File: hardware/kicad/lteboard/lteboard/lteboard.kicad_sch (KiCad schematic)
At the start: 0 parts

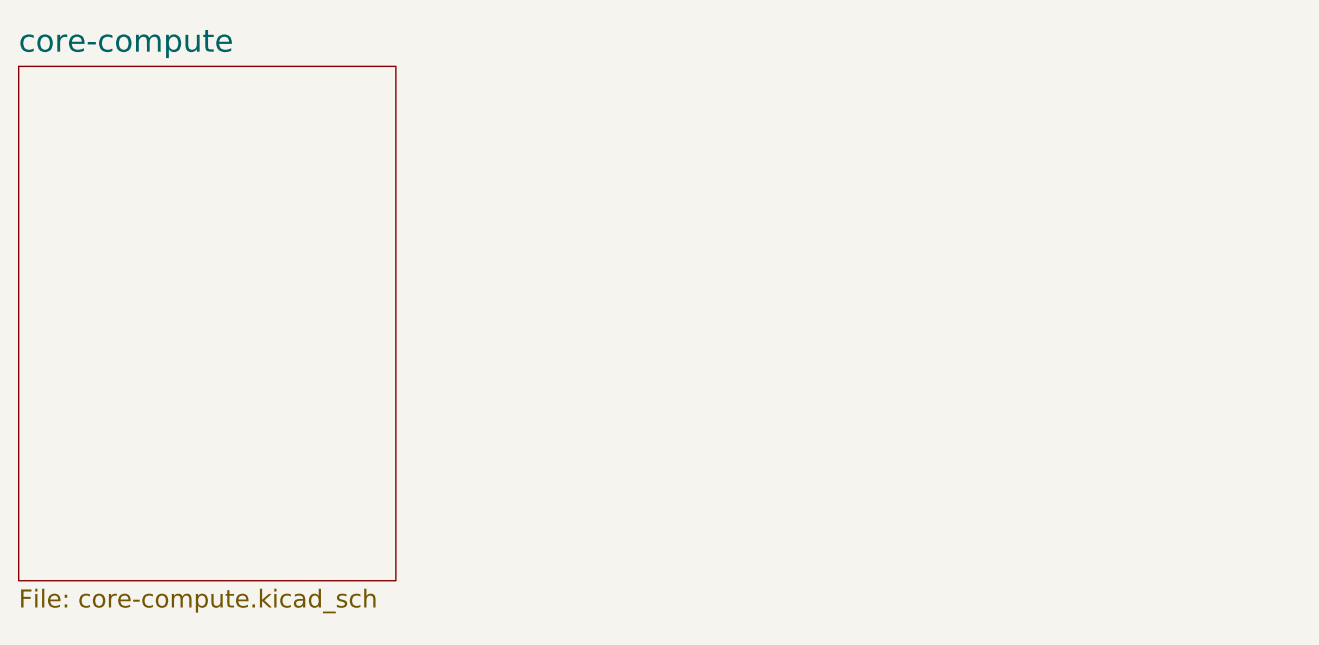
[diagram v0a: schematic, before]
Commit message: status-indication: fix GND_LOGIC scope, add sheet + PCA9535PW component placement
- core-compute.kicad_sch: converted 5 local GND_LOGIC labels to global_label,
  matching the project convention (global labels reserved for GND_LOGIC only).
  Local scope would have left the new status-indication sheet's GND_LOGIC
  electrically isolated from the MCU's ground - a real bug caught before wiring.
- lteboard.kicad_sch / lteboard.kicad_pro: added the new status_indication
  hierarchical sheet as LTEBOARD's second child sheet.
- status_indication.kicad_sch: new sheet, components placed (PCA9535PW I2C GPIO
  expander, 6x status LED, 6x 680R LED resistor, 2x 4.7k I2C pull-up, 1x 10k INT
  pull-up, 1x 100nF decoupling cap) - not yet wired.
- Added PCA9535PW symbol/footprint/3D-model library under hardware/kicad/lteboard/libs/
  (not in KiCad's default library) and the project's sym-lib-table pointing to it,
  fixed to use ${KIPRJMOD}-relative path instead of an absolute machine path.

Deliberately not included: uncommitted analog-io changes still sitting in this
working tree (power.kicad_sch, digital_inputs.kicad_sch, relay_outputs.kicad_sch,
ioboard.kicad_pro/kicad_sch, analog_io.kicad_sch) - this branch forked before
analog-io merged, and that content already lives on the analog-io branch.
Committing it here too would duplicate it across two branches.

Co-Authored-By: Claude Sonnet 5 <noreply@anthropic.com>
Claude-Session: https://claude.ai/code/session_011Mk4ACKLUzGL8p2SUjrweQ
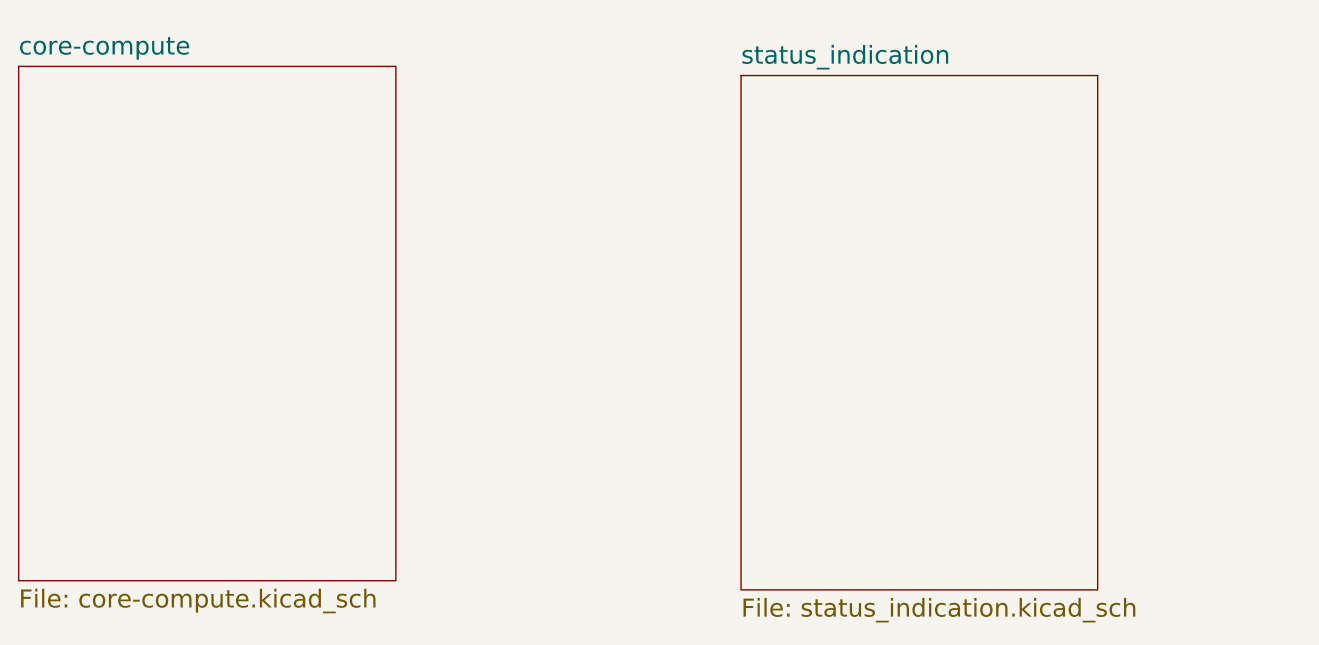
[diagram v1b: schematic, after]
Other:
- added sheet status_indication (status_indication.kicad_sch)
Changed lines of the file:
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@@
 		)
 		(property "Sheetname" "core-compute"
-			(at 35.56 36.7734 0)
+			(at 35.56 37.0234 0)
 			(effects
 				(font
-					(size 2.5 2.5)
+					(size 2 2)
 				)
 				(justify left bottom)
@@
 				)
 			)
+		)
+	)
+	(sheet
+		(at 115.824 39.116)
+		(size 39.624 57.15)
+		(exclude_from_sim no)
+		(in_bom yes)
+		(on_board yes)
+		(dnp no)
+		(fields_autoplaced yes)
+		(stroke
+			(width 0.1524)
+			(type solid)
+		)
+		(fill
+			(color 0 0 0 0.0000)
+		)
+		(property "Sheetname" "status_indication"
+			(at 115.824 38.0394 0)
+			(effects
+				(font
+					(size 2 2)
+				)
+				(justify left bottom)
+			)
+		)
+		(property "Sheetfile" "status_indication.kicad_sch"
+			(at 115.824 97.1426 0)
+			(effects
+				(font
+					(size 2 2)
+				)
+				(justify left top)
+			)
+		)
+		(instances
+			(project "lteboard"
+				(path "/e3cbe890-827c-4e3e-bf4e-d33595c4d0b3"
+					(page "3")
+				)
+			)

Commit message: status-indication: complete schematic capture, cross-sheet wiring, docs, and BOM
- status_indication.kicad_sch: full wiring completed (address straps, power/ground,
  I2C pull-ups, INT pull-up, decoupling, 6 LED channels). Caught and fixed two real bugs
  via full programmatic connectivity verification (every pin/net reconstructed from the
  actual file, not just visual inspection): all 6 LEDs were initially wired with reversed
  polarity (would never have lit), and a new hierarchical 3V3_LOGIC label was placed
  floating (same name, no wire, so not actually part of the net). 10 spare GPIOs marked
  with No-Connect flags.
- core-compute.kicad_sch: converted 5 local GND_LOGIC labels to global_label (same class
  of bug fixed in power.kicad_sch during analog-io's ERC pass -- would have left this new
  sheet's ground isolated from the MCU's). Added I2C_SDA/I2C_SCL (Bidirectional, on
  GPIO8/GPIO9) and 3V3_LOGIC (Passive) hierarchical labels for cross-sheet export.
  Confirmed J1's 4 VBUS pins share one schematic pin location by symbol design, so the
  existing single No-Connect flag already covers all 4 -- no gap there.
- lteboard.kicad_sch: wired the two sheet symbols together (I2C_SDA, I2C_SCL, 3V3_LOGIC),
  verified pin types match on both ends (Passive/Passive, Bidirectional/Bidirectional x2)
  and wire endpoints land exactly on the corresponding pins.
- Added docs/subsystems/status-indication.md (full build-plan writeup, Steps 1-8) and
  hardware/bom/status_indication_bom.csv (10 parts).
- docs/roadmap.md: item 5 (status indication) marked DONE; backfilled item 4 (relay
  outputs) to DONE too, since it was already complete but never marked here.
- docs/build-log.md: added the status-indication entry, and backfilled the relay-outputs
  entry that was missing.

ERC deferred to a single project-wide pass once every subsystem is built, per current
project decision (not run per-subsystem here, unlike analog-io).

Deliberately not included: uncommitted analog-io changes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
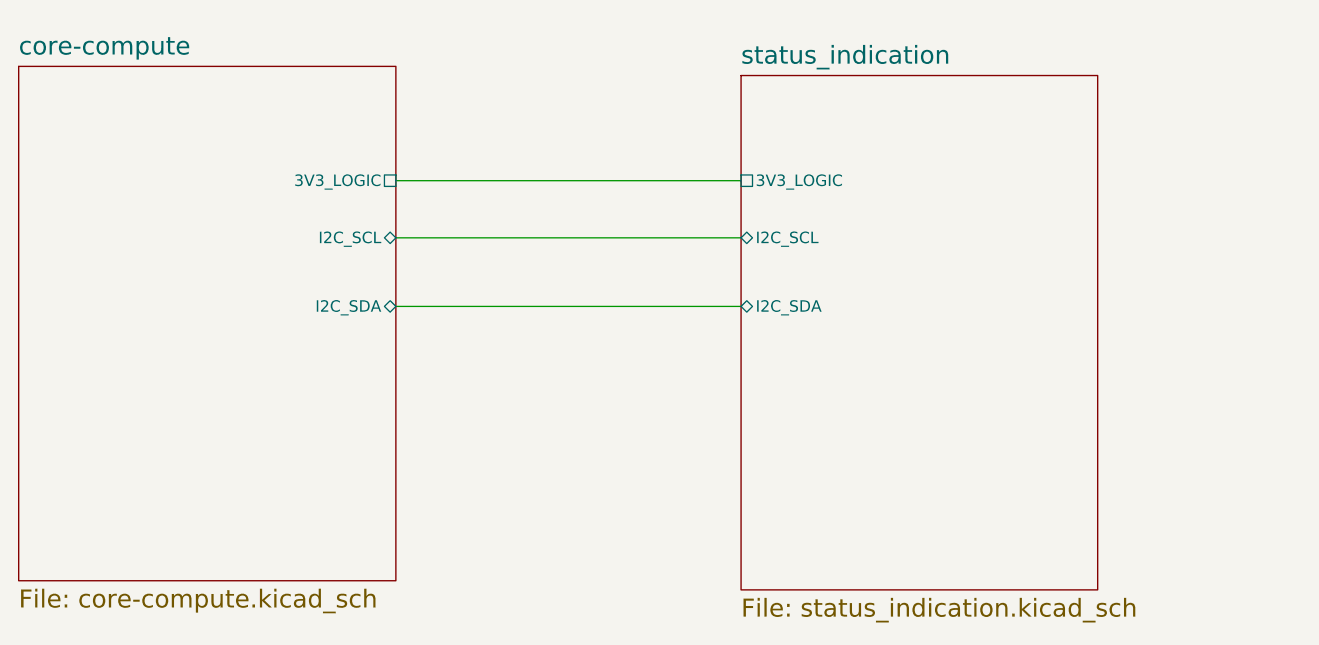
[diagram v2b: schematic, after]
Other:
- sheet core-compute ports: added 3V3_LOGIC, I2C_SCL, I2C_SDA; removed none
- sheet status_indication ports: added 3V3_LOGIC, I2C_SCL, I2C_SDA; removed none
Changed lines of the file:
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@@
 	(generator_version "9.0")
 	(paper "A4")
+	(wire
+		(pts
+			(xy 77.47 50.8) (xy 115.824 50.8)
+		)
+		(stroke
+			(width 0)
+			(type default)
+		)
+	)
+	(wire
+		(pts
+			(xy 77.47 64.77) (xy 115.824 64.77)
+		)
+		(stroke
+			(width 0)
+			(type default)
+		)
+	)
+	(wire
+		(pts
+			(xy 77.47 57.15) (xy 115.824 57.15)
+		)
+		(stroke
+			(width 0)
+			(type default)
+		)
+	)
 	(sheet
 		(at 35.56 38.1)
@@
 				)
 				(justify left top)
+			)
+		)
+		(pin "3V3_LOGIC" passive
+			(at 77.47 50.8 0)
+			(effects
+				(font
+					(size 1.27 1.27)
+				)
+				(justify right)
+			)
+		)
+		(pin "I2C_SCL" bidirectional
+			(at 77.47 57.15 0)
+			(effects
+				(font
+					(size 1.27 1.27)
+				)
+				(justify right)
+			)
+		)
+		(pin "I2C_SDA" bidirectional
+			(at 77.47 64.77 0)
+			(effects
+				(font
+					(size 1.27 1.27)
+				)
+				(justify right)
 			)
 		)
@@
 			)
 		)
+		(pin "3V3_LOGIC" passive
+			(at 115.824 50.8 180)
+			(effects
+				(font
+					(size 1.27 1.27)
+				)
+				(justify left)
+			)
+		)
+		(pin "I2C_SCL" bidirectional
+			(at 115.824 57.15 180)
+			(effects
+				(font
+					(size 1.27 1.27)
+				)
+				(justify left)
+			)
+		)
+		(pin "I2C_SDA" bidirectional
+			(at 115.824 64.77 180)
+			(effects
+				(font
+					(size 1.27 1.27)
+				)
+				(justify left)
+			)
+		)
